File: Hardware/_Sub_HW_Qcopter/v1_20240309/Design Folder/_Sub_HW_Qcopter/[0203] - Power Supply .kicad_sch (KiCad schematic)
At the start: 14 parts, among them J501 HDR_1X2_VERT, U501 TLV70313DBVR, U502 TLV70328DBVR

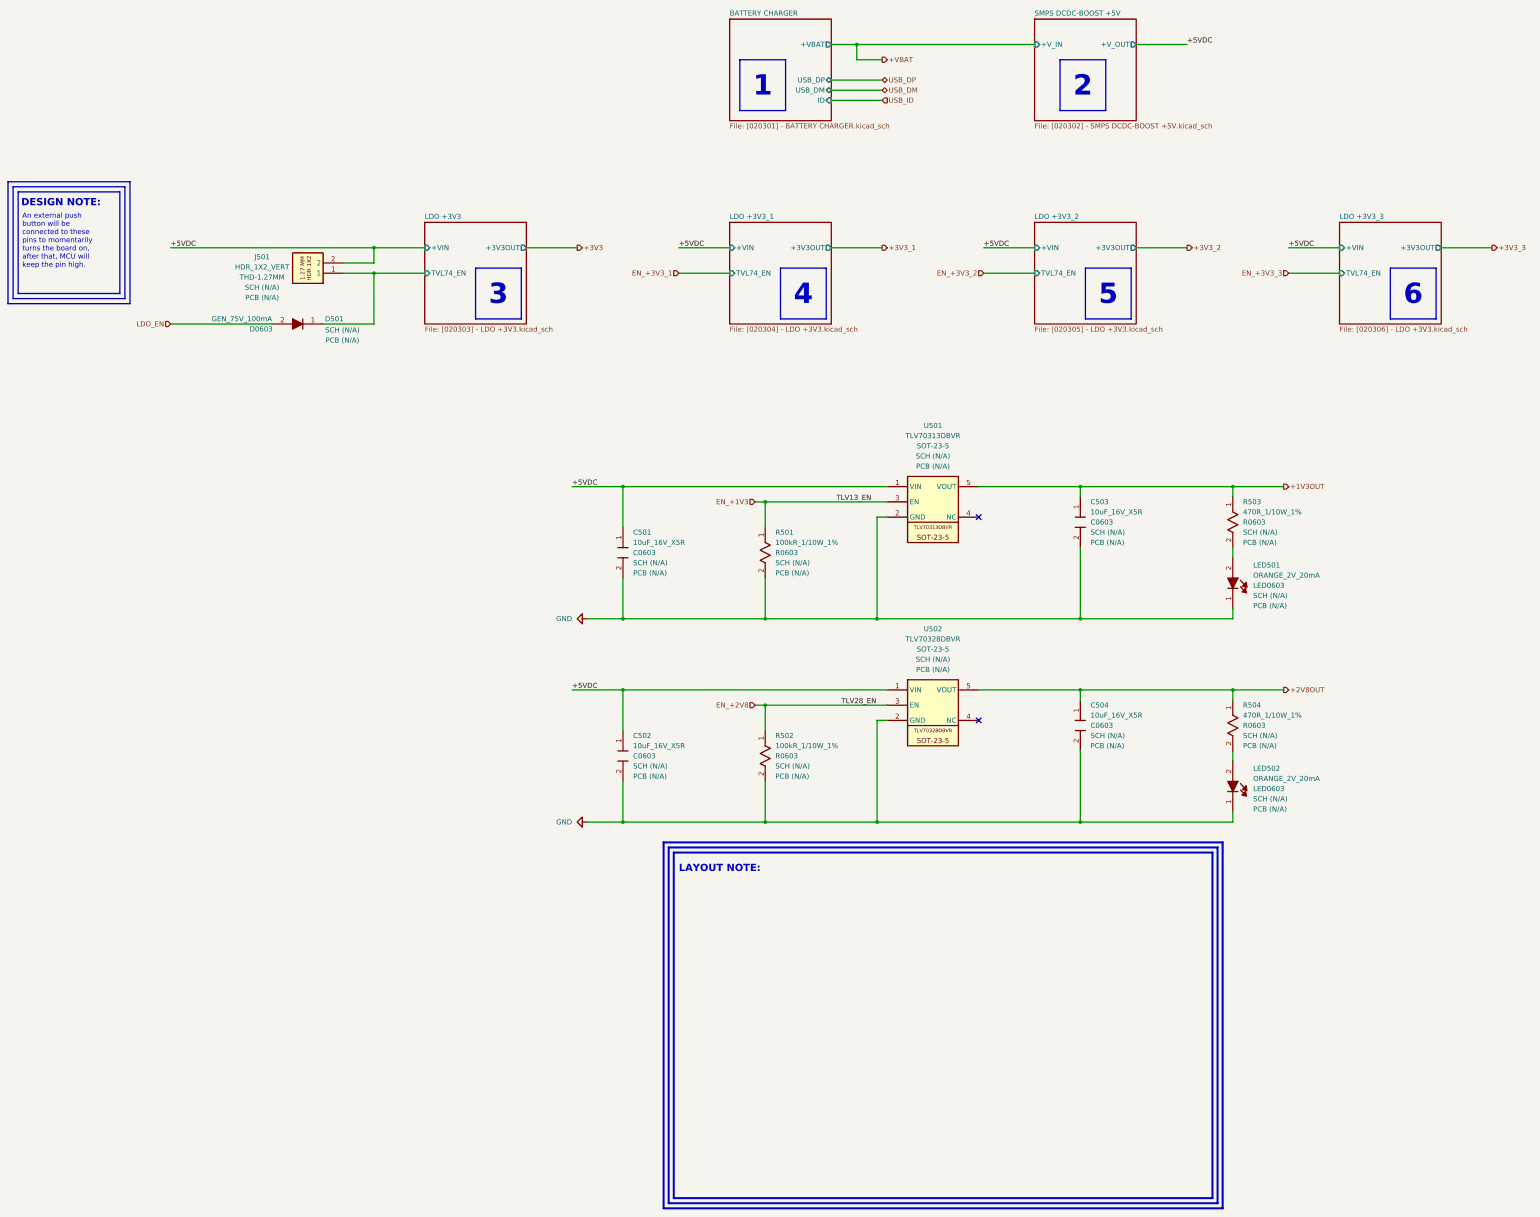
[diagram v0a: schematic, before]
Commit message: Update [0203] - Power Supply .kicad_sch
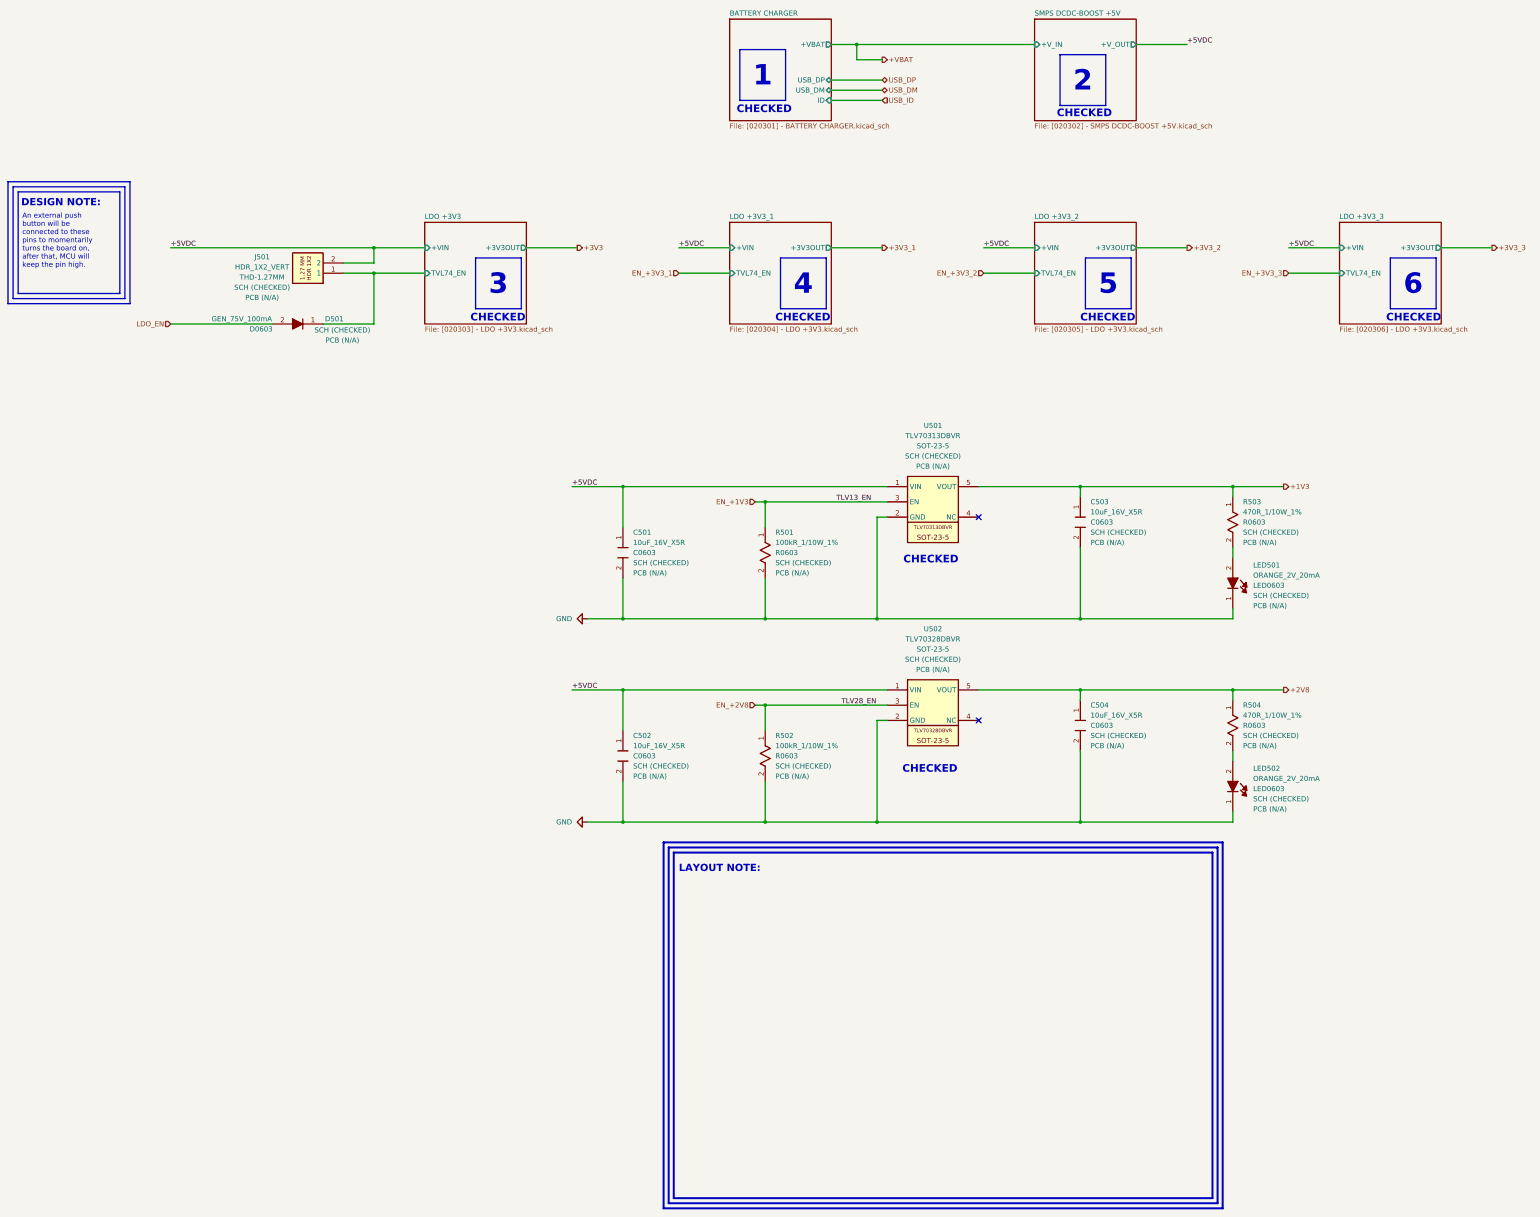
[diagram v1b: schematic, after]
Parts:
- C501, C502, C503, C504, D501, J501, LED501, LED502, R501, R502, R503, R504, U501, U502: SCH CHECK SCH (N/A) -> SCH (CHECKED)
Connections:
- net +1V3OUT renamed +1V3
- net +2V8OUT renamed +2V8
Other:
- note added: "CHECKED"
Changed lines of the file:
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@@
 	(title_block
 		(title "Quadcopter")
-		(date "2024-03-17")
+		(date "2024-03-18")
 		(rev "01")
 		(company "Mend0z0")
 		(comment 1 "01")
-		(comment 2 "PRELIMINARY")
+		(comment 2 "CHECKED")
 		(comment 3 "Siavash Taher Parvar")
 		(comment 8 "N/A")
@@
 	(text_box "6"
 		(exclude_from_sim no)
-		(at 368.3 163.83 0)
+		(at 368.3 161.29 0)
 		(size 11.43 12.7)
 		(stroke
@@
 	(text_box "5"
 		(exclude_from_sim no)
-		(at 292.1 163.83 0)
+		(at 292.1 161.29 0)
 		(size 11.43 12.7)
 		(stroke
@@
 	(text_box "4"
 		(exclude_from_sim no)
-		(at 215.9 163.83 0)
+		(at 215.9 161.29 0)
 		(size 11.43 12.7)
 		(stroke
@@
 	(text_box "1"
 		(exclude_from_sim no)
-		(at 205.74 111.76 0)
+		(at 205.74 109.22 0)
 		(size 11.43 12.7)
 		(stroke
@@
 	(text_box "2"
 		(exclude_from_sim no)
-		(at 285.75 111.76 0)
+		(at 285.75 110.49 0)
 		(size 11.43 12.7)
 		(stroke
@@
 	(text_box "3"
 		(exclude_from_sim no)
-		(at 139.7 163.83 0)
+		(at 139.7 161.29 0)
 		(size 11.43 12.7)
 		(stroke
@@
 		)
 	)
+	(text "CHECKED"
+		(exclude_from_sim no)
+		(at 374.142 176.276 0)
+		(effects
+			(font
+				(size 1.905 1.905)
+				(thickness 0.381)
+				(bold yes)
+			)
+		)
+	)
+	(text "CHECKED"
+		(exclude_from_sim no)
+		(at 253.492 236.728 0)
+		(effects
+			(font
+				(size 1.905 1.905)
+				(thickness 0.381)
+				(bold yes)
+			)
+		)
+	)
+	(text "CHECKED"
+		(exclude_from_sim no)
+		(at 145.288 176.276 0)
+		(effects
+			(font
+				(size 1.905 1.905)
+				(thickness 0.381)
+				(bold yes)
+			)
+		)
+	)
 	(text "DESIGN NOTE:"
 		(exclude_from_sim no)
@@
 		)
 	)
+	(text "CHECKED"
+		(exclude_from_sim no)
+		(at 297.688 176.276 0)
+		(effects
+			(font
+				(size 1.905 1.905)
+				(thickness 0.381)
+				(bold yes)
+			)
+		)
+	)
+	(text "CHECKED"
+		(exclude_from_sim no)
+		(at 221.488 176.276 0)
+		(effects
+			(font
+				(size 1.905 1.905)
+				(thickness 0.381)
+				(bold yes)
+			)
+		)
+	)
 	(text "LAYOUT NOTE:"
 		(exclude_from_sim no)
@@
 		)
 	)
+	(text "CHECKED"
+		(exclude_from_sim no)
+		(at 253.238 289.052 0)
+		(effects
+			(font
+				(size 1.905 1.905)
+				(thickness 0.381)
+				(bold yes)
+			)
+		)
+	)
+	(text "CHECKED"
+		(exclude_from_sim no)
+		(at 291.846 125.222 0)
+		(effects
+			(font
+				(size 1.905 1.905)
+				(thickness 0.381)
+				(bold yes)
+			)
+		)
+	)
+	(text "CHECKED"
+		(exclude_from_sim no)
+		(at 211.836 124.206 0)
+		(effects
+			(font
+				(size 1.905 1.905)
+				(thickness 0.381)
+				(bold yes)
+			)
+		)
+	)
 	(label "+5VDC"
 		(at 63.5 158.75 0)
@@
 		)
 	)
-	(hierarchical_label "+2V8OUT"
+	(hierarchical_label "+2V8"
 		(shape output)
 		(at 341.63 269.24 0)
@@
 		)
 	)
-	(hierarchical_label "+1V3OUT"
+	(hierarchical_label "+1V3"
 		(shape output)
 		(at 341.63 218.44 0)
@@
 			)
 		)
-		(property "SCH CHECK" "SCH (N/A)"
+		(property "SCH CHECK" "SCH (CHECKED)"
 			(at 254 261.62 0)
 			(effects
@@
 			)
 		)
-		(property "SCH CHECK" "SCH (N/A)"
+		(property "SCH CHECK" "SCH (CHECKED)"
 			(at 331.47 280.6699 90)
 			(effects
@@
 			)
 		)
-		(property "SCH CHECK" "SCH (N/A)"
+		(property "SCH CHECK" "SCH (CHECKED)"
 			(at 334.01 296.4814 90)
 			(effects
@@
 			)
 		)
-		(property "SCH CHECK" "SCH (N/A)"
+		(property "SCH CHECK" "SCH (CHECKED)"
 			(at 254 210.82 0)
 			(effects
@@
 			)
 		)
-		(property "SCH CHECK" "SCH (N/A)"
+		(property "SCH CHECK" "SCH (CHECKED)"
 			(at 293.37 229.8699 90)
 			(effects
@@
 			)
 		)
-		(property "SCH CHECK" "SCH (N/A)"
+		(property "SCH CHECK" "SCH (CHECKED)"
 			(at 331.47 229.8699 90)
 			(effects
@@
 			)
 		)
-		(property "SCH CHECK" "SCH (N/A)"
+		(property "SCH CHECK" "SCH (CHECKED)"
 			(at 86.36 168.656 0)
 			(effects
@@
 			)
 		)
-		(property "SCH CHECK" "SCH (N/A)"
+		(property "SCH CHECK" "SCH (CHECKED)"
 			(at 179.07 237.4899 90)
 			(effects
@@
 			)
 		)
-		(property "SCH CHECK" "SCH (N/A)"
+		(property "SCH CHECK" "SCH (CHECKED)"
 			(at 214.63 288.2899 90)
 			(effects
@@
 			)
 		)
-		(property "SCH CHECK" "SCH (N/A)"
+		(property "SCH CHECK" "SCH (CHECKED)"
 			(at 293.37 280.6699 90)
 			(effects
@@
 			)
 		)
-		(property "SCH CHECK" "SCH (N/A)"
+		(property "SCH CHECK" "SCH (CHECKED)"
 			(at 334.01 245.6814 90)
 			(effects
@@
 			)
 		)
-		(property "SCH CHECK" "SCH (N/A)"
+		(property "SCH CHECK" "SCH (CHECKED)"
 			(at 179.07 288.2899 90)
 			(effects
@@
 			)
 		)
-		(property "SCH CHECK" "SCH (N/A)"
+		(property "SCH CHECK" "SCH (CHECKED)"
 			(at 106.426 179.324 0)
 			(effects
@@
 			)
 		)
-		(property "SCH CHECK" "SCH (N/A)"
+		(property "SCH CHECK" "SCH (CHECKED)"
 			(at 214.63 237.4899 90)
 			(effects

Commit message: Update [0203] - Power Supply .kicad_sch
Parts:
- removed LED501, LED502: ORANGE_2V_20mA, LED_SMD:LED_0603_1608Metric, symbol _SCHLIB_Qcopter:DIODE_LED_ORANGE_2V_20mA_611nm_LED0603
- removed R503, R504: 470R_1/10W_1%, Resistor_SMD:R_0603_1608Metric, symbol _SCHLIB_Qcopter:RES_470R_1/10W_1%_R0603
